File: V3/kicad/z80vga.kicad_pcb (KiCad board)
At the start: 2 copper layers, 129.5 x 86.4 mm, 60 parts, among them J1000 Barrel_Jack_Switch, J2100 Conn_02x24_Odd_Even, J2101 Conn_01x02_Male, J2120 USB_B, J2121 Conn_01x03_Male, J2122 Conn_01x02_Male, J2200 Conn_01x08_Male, J2201 Conn_01x08_Male, J2210 Micro_SD_Card_Det, J2220 AVR-ISP-6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

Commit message: still trying to make routes work
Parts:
- removed J2100: Conn_02x24_Odd_Even, Connector_PinSocket_2.54mm:PinSocket_2x24_P2.54mm_Vertical
- moved C2200 9.67 mm to (134.6, 77.5)
- moved C2101 7.62 mm to (139.7, 104.1)
- moved D2101 6.35 mm to (153.7, 127.0)
- moved D2100 6.35 mm to (158.8, 127.0)
- moved U3000 5.24 mm to (105.4, 86.4)
- moved C3000 5.08 mm to (97.8, 87.6)
- moved C3001 5.08 mm to (119.4, 81.3)
- moved U2101 5.08 mm to (128.3, 101.6)
- moved U3001 5.08 mm to (92.7, 102.9)
- moved X2100 4.58 mm to (148.6, 119.4)
- moved RN2100 4.02 mm to (133.3, 72.4)
- moved U2200 3.81 mm to (133.3, 87.6)
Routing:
- net /2000_Z80/WRITE: track 0.00 -> 57.6 mm, vias 0 -> 2
- net /2000_Z80/READ: track 0.00 -> 45.0 mm, vias 0 -> 1
- net /2000_Z80/RAM_CS: track 0.00 -> 44.5 mm, vias 0 -> 1
- net +5V: track 131.0 -> 95.3 mm, vias 1 -> 2
- net /3000_Memory/A14: track 0.00 -> 34.3 mm, vias 0 -> 1
- net /3000_Memory/D3: track 0.00 -> 29.9 mm
- net /3000_Memory/D4: track 0.00 -> 29.3 mm
- net /3000_Memory/D5: track 0.00 -> 28.0 mm
- net /3000_Memory/D6: track 0.00 -> 26.7 mm
- net /3000_Memory/D7: track 0.00 -> 25.2 mm
- net /3000_Memory/A10: track 0.00 -> 25.1 mm
- net /3000_Memory/A17: track 0.00 -> 24.2 mm
- net /3000_Memory/A11: track 0.00 -> 24.1 mm
- net /3000_Memory/A9: track 0.00 -> 23.5 mm
- net /3000_Memory/A13: track 0.00 -> 23.1 mm
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
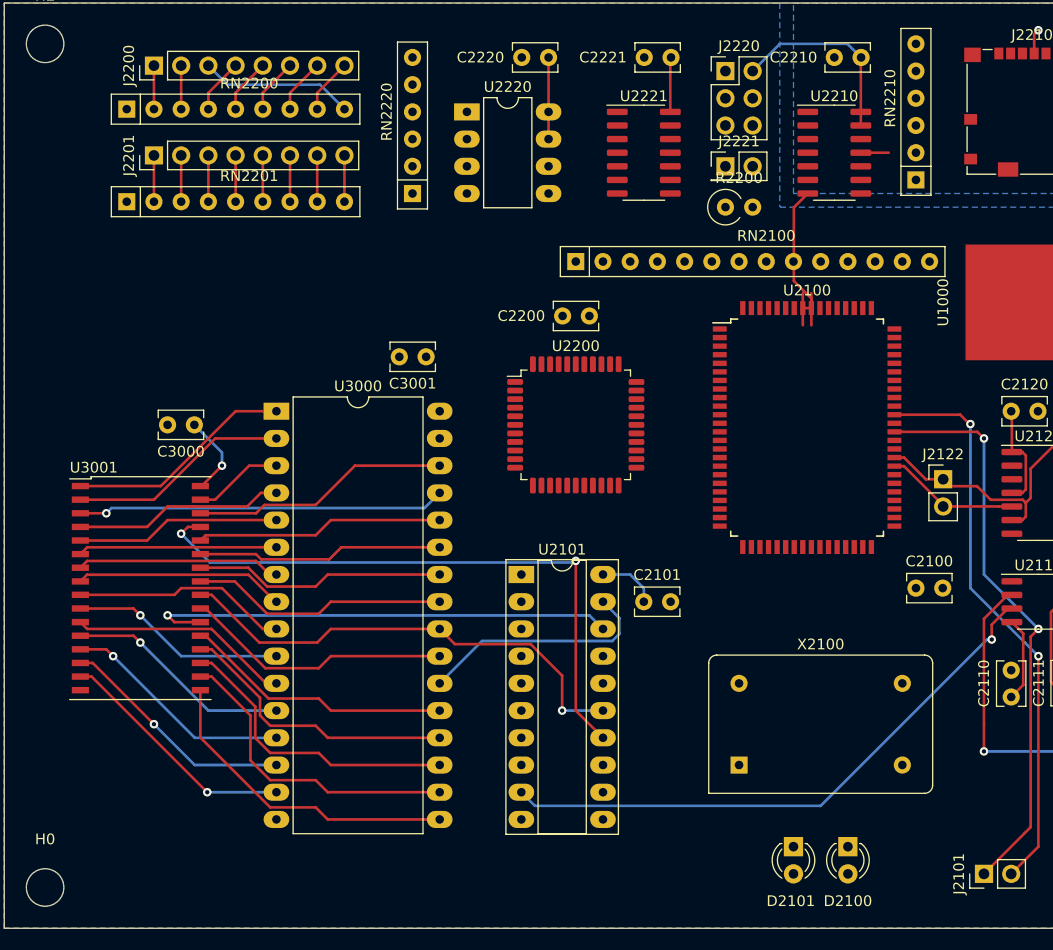
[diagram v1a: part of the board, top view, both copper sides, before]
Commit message: fixed up PIO routing
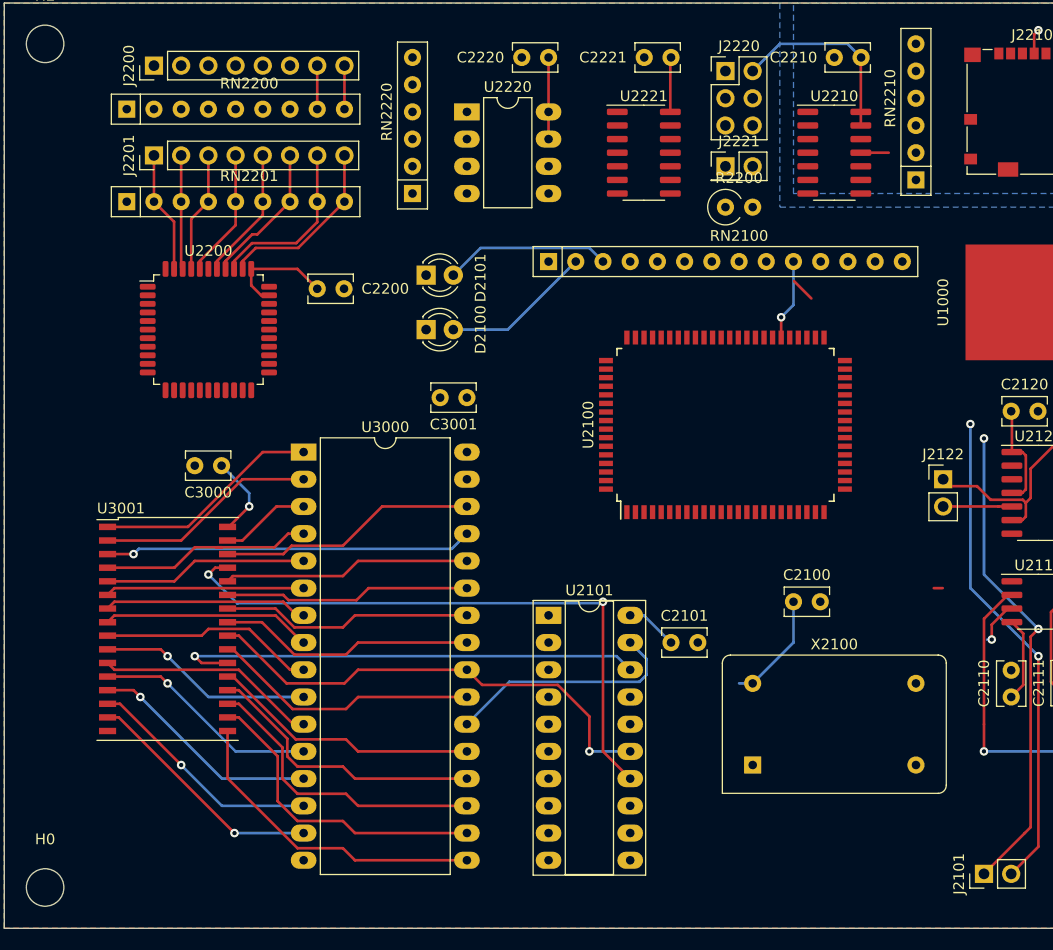
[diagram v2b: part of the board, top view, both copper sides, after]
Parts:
- moved D2101 63.4 mm to (119.4, 73.7), turned to 0 degrees
- moved D2100 62.3 mm to (119.4, 78.7), turned to 0 degrees
- moved U2200 35.4 mm to (99.1, 78.7)
- moved C2200 25.5 mm to (109.2, 74.9), turned to 0 degrees
- moved C2100 11.5 mm to (153.7, 104.1)
- moved U2100 7.62 mm to (147.3, 87.6), turned to 90 degrees
- moved C3001 5.39 mm to (123.2, 85.1)
- moved C2101 4.58 mm to (142.2, 108.0)
- moved C3000 4.58 mm to (100.3, 91.4)
- moved U3000 4.58 mm to (108.0, 90.2)
- moved U3001 4.58 mm to (95.2, 106.7)
- moved U2101 4.58 mm to (130.8, 105.4)
- moved RN2100 2.54 mm to (130.8, 72.4)
- moved X2100 1.27 mm to (149.9, 119.4)
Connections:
- J2200 pad 1: /2000_Z80/2200_PERP_ALT/MISO -> /2000_Z80/2200_PERP_ALT/CS4
- J2200 pad 2: /2000_Z80/2200_PERP_ALT/SCK -> /2000_Z80/2200_PERP_ALT/CS3
- J2200 pad 3: /2000_Z80/2200_PERP_ALT/MOSI -> /2000_Z80/2200_PERP_ALT/CS2
- J2200 pad 4: /2000_Z80/2200_PERP_ALT/CS0 -> /2000_Z80/2200_PERP_ALT/CS1
- J2200 pad 5: /2000_Z80/2200_PERP_ALT/CS1 -> /2000_Z80/2200_PERP_ALT/CS0
- J2200 pad 6: /2000_Z80/2200_PERP_ALT/CS2 -> /2000_Z80/2200_PERP_ALT/MOSI
- J2200 pad 7: /2000_Z80/2200_PERP_ALT/CS3 -> /2000_Z80/2200_PERP_ALT/SCK
- J2200 pad 8: /2000_Z80/2200_PERP_ALT/CS4 -> /2000_Z80/2200_PERP_ALT/MISO
- RN2200 pad 2: /2000_Z80/2200_PERP_ALT/MISO -> /2000_Z80/2200_PERP_ALT/MOSI
- RN2200 pad 3: /2000_Z80/2200_PERP_ALT/SCK -> /2000_Z80/2200_PERP_ALT/CS4
- RN2200 pad 4: /2000_Z80/2200_PERP_ALT/CS0 -> /2000_Z80/2200_PERP_ALT/CS3
- RN2200 pad 5: /2000_Z80/2200_PERP_ALT/CS1 -> /2000_Z80/2200_PERP_ALT/CS2
- RN2200 pad 6: /2000_Z80/2200_PERP_ALT/CS2 -> /2000_Z80/2200_PERP_ALT/CS1
- RN2200 pad 7: /2000_Z80/2200_PERP_ALT/CS3 -> /2000_Z80/2200_PERP_ALT/CS0
- RN2200 pad 8: /2000_Z80/2200_PERP_ALT/CS4 -> /2000_Z80/2200_PERP_ALT/SCK
- RN2200 pad 9: /2000_Z80/2200_PERP_ALT/MOSI -> /2000_Z80/2200_PERP_ALT/MISO
- U2100 pad 10: /3000_Memory/D2 -> /3000_Memory/A2
- U2100 pad 11: /3000_Memory/D3 -> /3000_Memory/A3
- U2100 pad 13: /3000_Memory/D4 -> /3000_Memory/A4
- U2100 pad 15: /3000_Memory/D5 -> /3000_Memory/A5
- U2100 pad 16: /3000_Memory/D6 -> /3000_Memory/A6
- U2100 pad 17: /3000_Memory/D7 -> /3000_Memory/A7
- U2100 pad 18: /2000_Z80/2100_ALTCPU/A8 -> /3000_Memory/A8
- U2100 pad 19: /2000_Z80/2100_ALTCPU/A9 -> /3000_Memory/A9
- U2100 pad 20: /2000_Z80/2100_ALTCPU/A10 -> /3000_Memory/A10
- U2100 pad 21: /2000_Z80/2100_ALTCPU/A11 -> /3000_Memory/A11
- U2100 pad 24: /2000_Z80/2100_ALTCPU/A12 -> /3000_Memory/A12
- U2100 pad 25: /2000_Z80/2100_ALTCPU/A13 -> /3000_Memory/A13
- U2100 pad 26: /2000_Z80/2100_ALTCPU/A14 -> /3000_Memory/A14
- U2100 pad 27: /2000_Z80/2100_ALTCPU/A15 -> /3000_Memory/A15
- U2100 pad 28: /2000_Z80/2100_ALTCPU/A16 -> /3000_Memory/A16
- U2100 pad 29: /2000_Z80/2100_ALTCPU/A17 -> /3000_Memory/A17
- U2100 pad 31: /2000_Z80/2100_ALTCPU/A18 -> /3000_Memory/A18
- U2100 pad 35: /3000_Memory/A0 -> /3000_Memory/D0
- U2100 pad 36: /3000_Memory/A1 -> /3000_Memory/D1
- U2100 pad 37: /3000_Memory/A2 -> /3000_Memory/D2
- U2100 pad 38: /3000_Memory/A3 -> /3000_Memory/D3
- U2100 pad 39: /3000_Memory/A4 -> /3000_Memory/D4
- U2100 pad 40: /3000_Memory/A5 -> /3000_Memory/D5
- U2100 pad 41: /3000_Memory/A6 -> /3000_Memory/D6
- U2100 pad 44: /3000_Memory/A7 -> /3000_Memory/D7
- U2100 pad 8: /3000_Memory/D0 -> /3000_Memory/A0
- U2100 pad 9: /3000_Memory/D1 -> /3000_Memory/A1
- U2101 pad 6: /3000_Memory/D7 -> /3000_Memory/A7
- U2101 pad 7: /2000_Z80/2100_ALTCPU/A18 -> /3000_Memory/A18
- U2200 pad 11: /3000_Memory/D1 -> /3000_Memory/A1
- U2200 pad 12: /3000_Memory/D0 -> /3000_Memory/A0
- U2200 pad 26: /3000_Memory/A0 -> /3000_Memory/D0
- U2200 pad 27: /3000_Memory/A1 -> /3000_Memory/D1
- U2200 pad 4: /3000_Memory/A5 -> /3000_Memory/D5
- U2200 pad 5: /3000_Memory/A4 -> /3000_Memory/D4
- U2200 pad 6: /3000_Memory/A3 -> /3000_Memory/D3
- U2200 pad 7: /3000_Memory/A2 -> /3000_Memory/D2
- U2200 pad 8: /3000_Memory/A7 -> /3000_Memory/D7
- U2200 pad 9: /3000_Memory/A6 -> /3000_Memory/D6
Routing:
- net /2000_Z80/2100_ALTCPU/2110_Reset/Reset: track 54.8 -> 4.33 mm
- net +5V: track 95.3 -> 115.5 mm
- net Net-(D2101-Pad2): track 0.00 -> 15.5 mm
- net GND: track 21.3 -> 5.79 mm
- net /2000_Z80/2200_PERP_ALT/MOSI: track 14.4 -> 0.00 mm
- net Net-(D2100-Pad2): track 0.00 -> 14.1 mm
- net Net-(J2201-Pad8): track 4.32 -> 16.8 mm
- net Net-(J2201-Pad7): track 4.32 -> 16.2 mm
- net Net-(J2201-Pad6): track 4.32 -> 13.4 mm
- net Net-(J2101-Pad1): track 53.5 -> 44.8 mm
- net Net-(J2201-Pad5): track 4.32 -> 12.4 mm
- net Net-(J2201-Pad4): track 4.32 -> 12.0 mm
- net /2000_Z80/2100_ALTCPU/CTS0: track 0.00 -> 7.57 mm, vias 0 -> 1
- net Net-(J2101-Pad2): track 53.1 -> 45.7 mm
- net Net-(J2201-Pad1): track 4.32 -> 11.4 mm
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
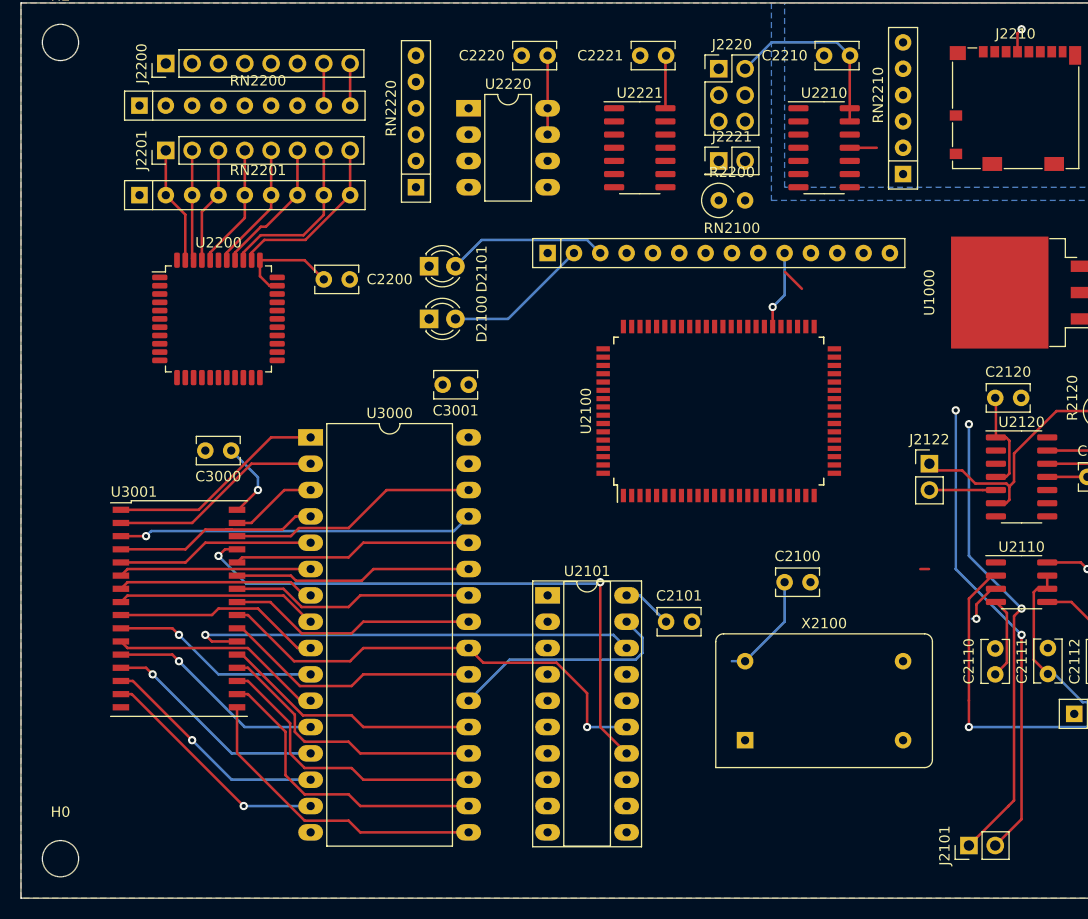
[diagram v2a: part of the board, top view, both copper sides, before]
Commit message: more PIO routing
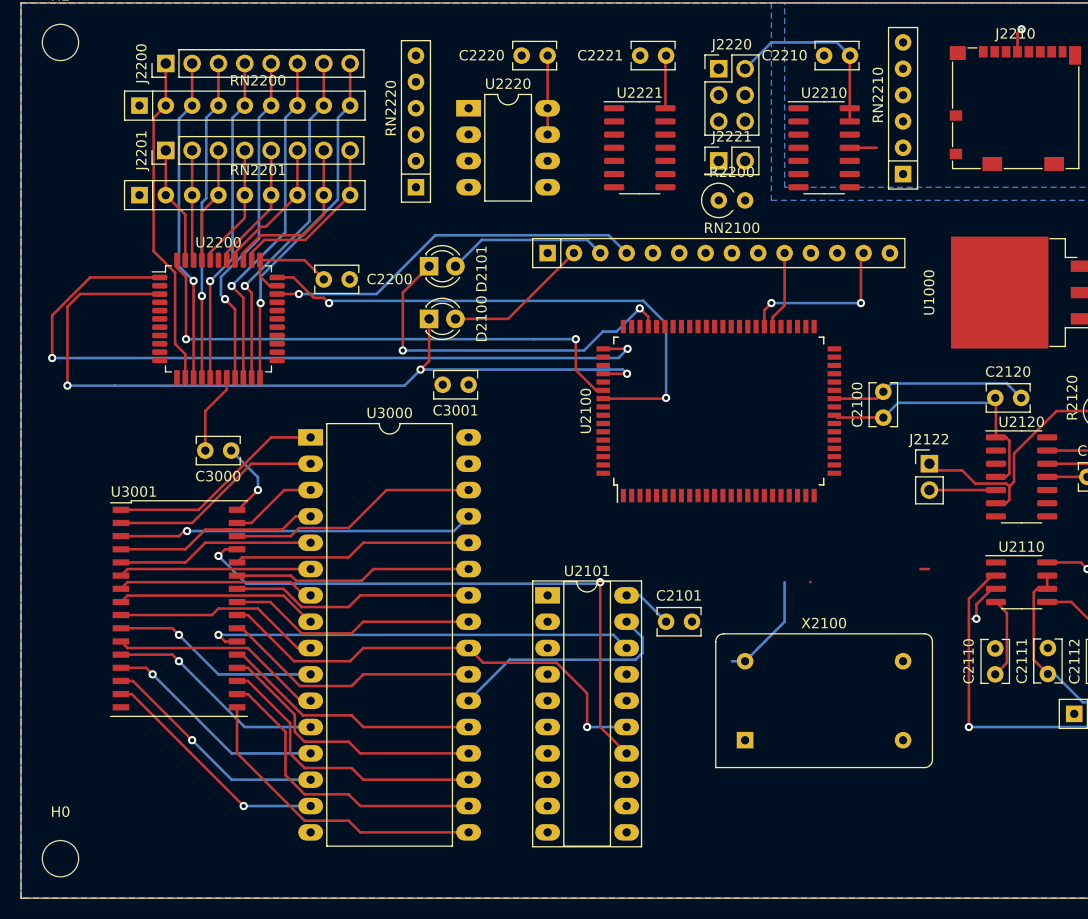
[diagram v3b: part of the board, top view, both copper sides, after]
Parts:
- removed J2101: Conn_01x02_Male, Connector_PinHeader_2.54mm:PinHeader_1x02_P2.54mm_Vertical
- moved C2100 18.5 mm to (163.2, 88.3), turned to 90 degrees
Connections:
- J2200 pad 1: /2000_Z80/2200_PERP_ALT/CS4 -> /2000_Z80/2200_PERP_ALT/MOSI
- J2200 pad 2: /2000_Z80/2200_PERP_ALT/CS3 -> /2000_Z80/2200_PERP_ALT/CS4
- J2200 pad 3: /2000_Z80/2200_PERP_ALT/CS2 -> /2000_Z80/2200_PERP_ALT/CS3
- J2200 pad 4: /2000_Z80/2200_PERP_ALT/CS1 -> /2000_Z80/2200_PERP_ALT/CS2
- J2200 pad 5: /2000_Z80/2200_PERP_ALT/CS0 -> /2000_Z80/2200_PERP_ALT/CS1
- J2200 pad 6: /2000_Z80/2200_PERP_ALT/MOSI -> /2000_Z80/2200_PERP_ALT/CS0
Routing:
- net /2000_Z80/2100_ALTCPU/M1: track 0.00 -> 79.4 mm, vias 0 -> 3
- net /2000_Z80/2100_ALTCPU/IORQ: track 0.00 -> 74.2 mm, vias 0 -> 2
- net /2000_Z80/2200_PERP_ALT/CLK: track 0.00 -> 52.8 mm, vias 0 -> 2
- net /2000_Z80/2100_ALTCPU/RD: track 0.00 -> 52.0 mm, vias 0 -> 2
- net Net-(U2100-Pad54): track 45.7 -> 0.00 mm, vias 2 -> 0
- net Net-(U2100-Pad52): track 44.8 -> 0.00 mm, vias 2 -> 0
- net /2000_Z80/2100_ALTCPU/INT: track 0.00 -> 36.8 mm, vias 0 -> 1
- net /2000_Z80/2100_ALTCPU/HALT: track 0.00 -> 35.8 mm, vias 0 -> 2
- net /2000_Z80/2200_PERP_ALT/CS0: track 0.00 -> 33.4 mm, vias 0 -> 1
- net /2000_Z80/2200_PERP_ALT/CS1: track 0.00 -> 32.9 mm, vias 0 -> 1
- net /2000_Z80/2200_PERP_ALT/MOSI: track 0.00 -> 32.1 mm
- net /2000_Z80/2200_PERP_ALT/CS2: track 0.00 -> 31.7 mm, vias 0 -> 1
- net /2000_Z80/2200_PERP_ALT/CS4: track 0.00 -> 31.4 mm, vias 0 -> 1
- net /2000_Z80/2200_PERP_ALT/CS3: track 0.00 -> 31.0 mm, vias 0 -> 1
- net /2000_Z80/2200_PERP_ALT/MISO: track 4.06 -> 33.9 mm, vias 0 -> 1
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
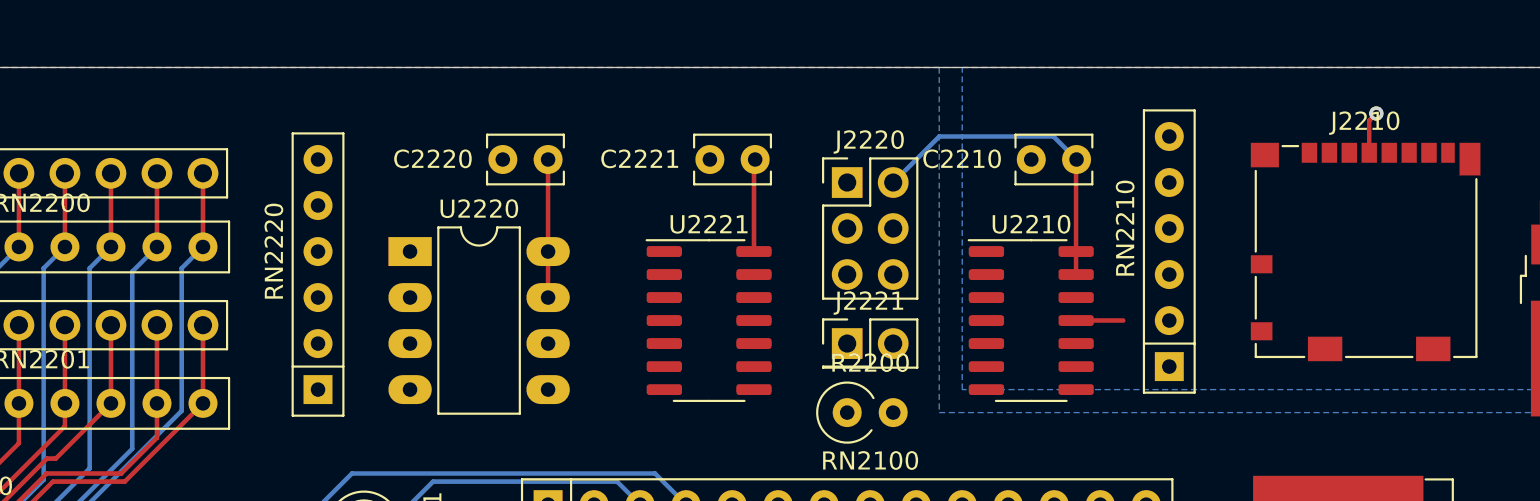
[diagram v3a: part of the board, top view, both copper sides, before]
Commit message: routing SD card control signals
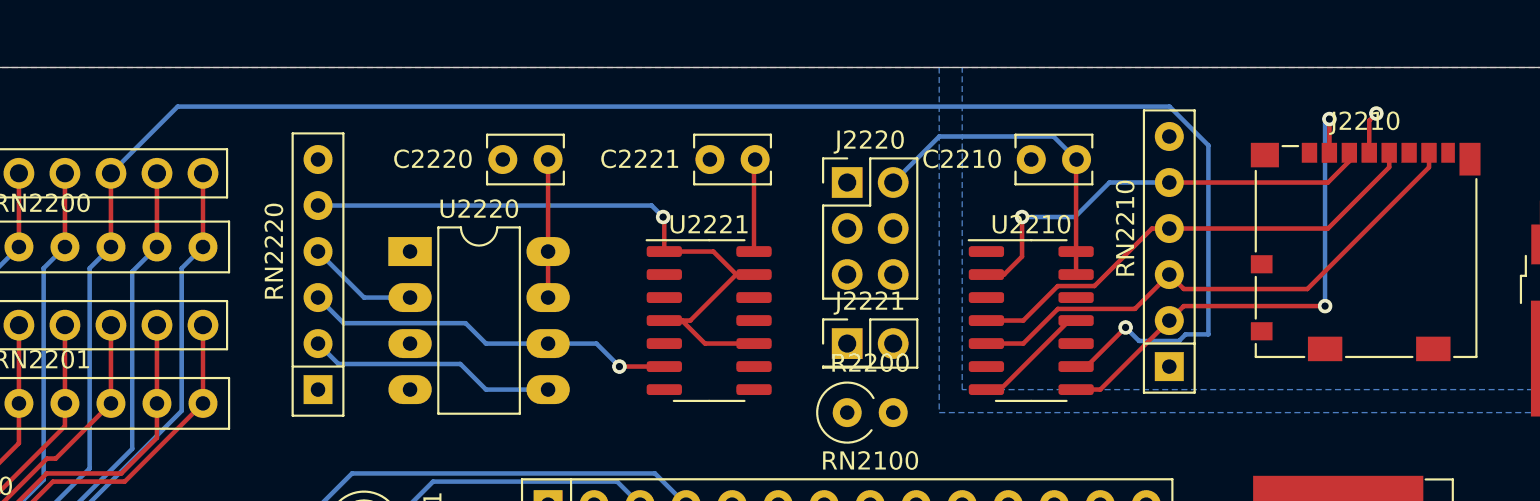
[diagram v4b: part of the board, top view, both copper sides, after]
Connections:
- RN2220 pad 5: /2000_Z80/2200_PERP_ALT/2220_ROM/LC_HOLD -> /2000_Z80/2200_PERP_ALT/2220_ROM/PROG_EN
- RN2220 pad 6: /2000_Z80/2200_PERP_ALT/2220_ROM/PROG_EN -> Net-(RN2220-Pad6)
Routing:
- net /2000_Z80/2200_PERP_ALT/CS0: track 33.4 -> 115.5 mm, vias 1 -> 2
- net /2000_Z80/2200_PERP_ALT/2220_ROM/PROG_EN: track 0.00 -> 37.2 mm, vias 0 -> 1
- net /2000_Z80/2200_PERP_ALT/2210_SD_Card/SD_MISO: track 0.00 -> 29.9 mm
- net /2000_Z80/2200_PERP_ALT/2210_SD_Card/SD_CS: track 0.00 -> 27.9 mm, vias 0 -> 2
- net /2000_Z80/2200_PERP_ALT/2210_SD_Card/SD_SCK: track 0.00 -> 26.5 mm
- net /2000_Z80/2200_PERP_ALT/2210_SD_Card/SD_MOSI: track 0.00 -> 24.4 mm, vias 0 -> 1
- net /2000_Z80/2200_PERP_ALT/2220_ROM/LC_SCK: track 0.00 -> 20.7 mm, vias 0 -> 1
- net /2000_Z80/2200_PERP_ALT/2220_ROM/LC_MOSI: track 0.00 -> 13.8 mm
- net /2000_Z80/2200_PERP_ALT/2220_ROM/LC_MISO: track 0.00 -> 6.13 mm
- net GND: track 30.6 -> 34.5 mm
